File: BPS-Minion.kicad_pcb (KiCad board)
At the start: 2 copper layers, 219 parts, among them J10 TopConn, J11 TopConn, J2 BMS1OTP, J3 BMS2OTP, J4 Conn_01x24_Female, J5 Conn_01x24_Female, J6 TopConn, J7 TopConn, J8 TopConn, J9 TopConn, U10 LM321, U11 ADS7953SBDBT, U12 MIC5317-2.5xM5, U2 BQ7695201PFBR, U3 ISO1640BDR, U4 EL3H7, U5 BQ7695201PFBR, U6 ISO1640BDR, U7 EL3H7, U8 LM321, U9 ADS7953SBDBT

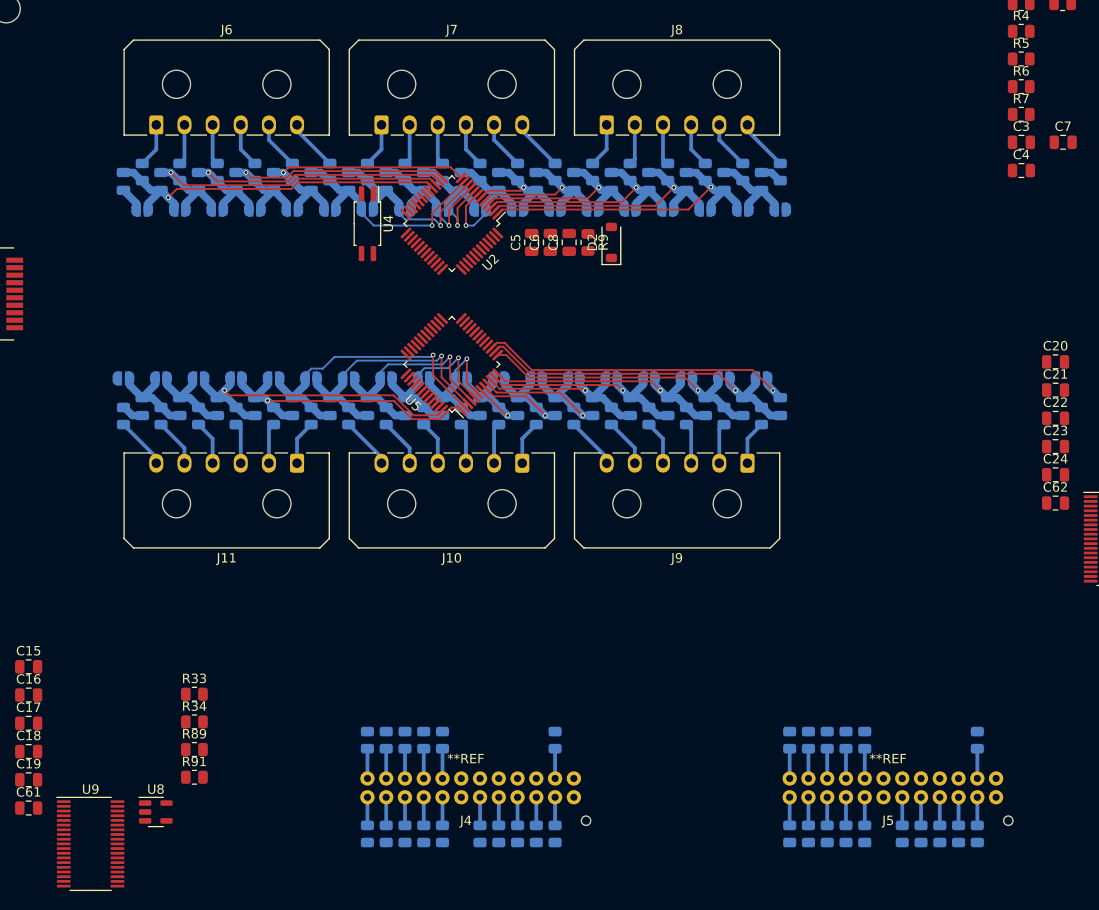
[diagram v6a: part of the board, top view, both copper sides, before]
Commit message: fix gnd2
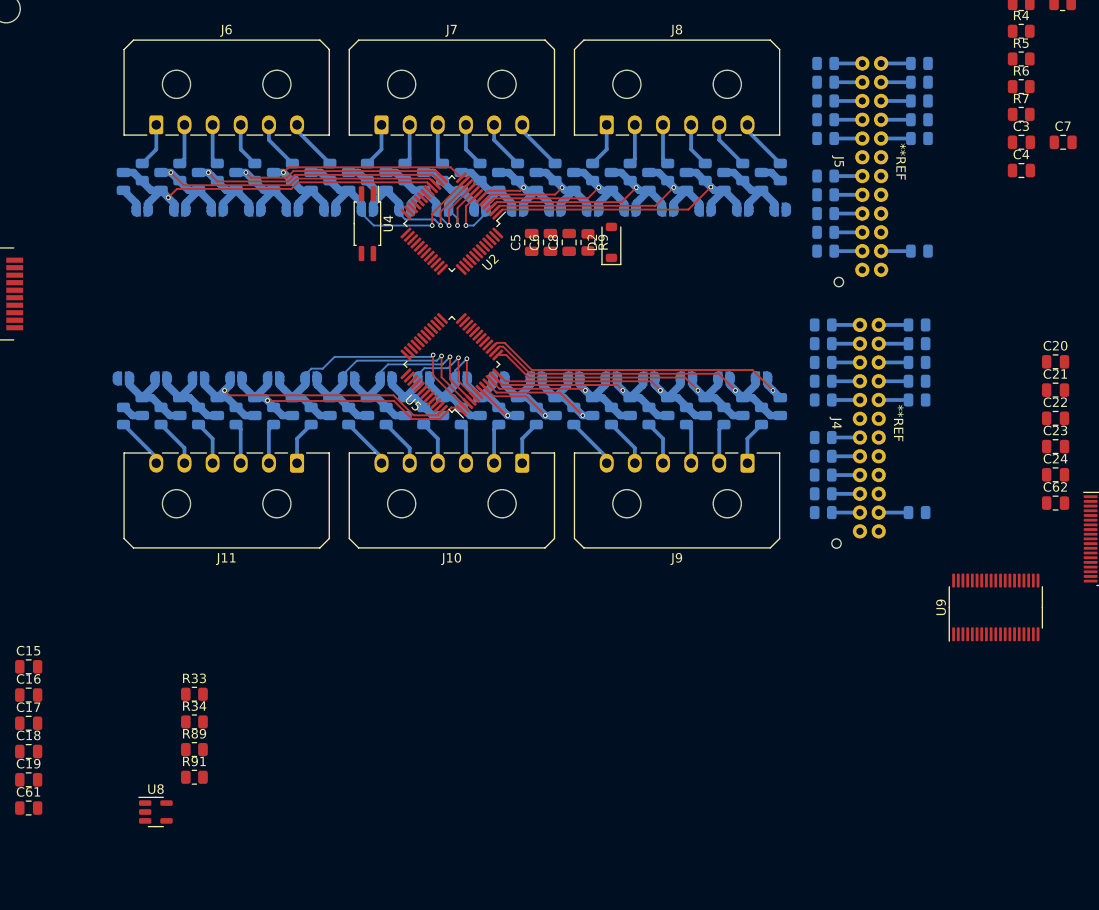
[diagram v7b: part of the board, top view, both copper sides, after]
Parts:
- moved U9 99.7 mm to (252.0, 152.4), turned to 90 degrees
- moved R43 82.2 mm to (233.8, 94.4), turned to 180 degrees
- moved R41 80.1 mm to (233.8, 96.4), turned to 180 degrees
- moved R39 78.1 mm to (233.8, 98.4), turned to 180 degrees
- moved R36 76.1 mm to (233.8, 100.4), turned to 180 degrees
- moved R38 74.2 mm to (233.8, 102.4), turned to 180 degrees
- moved R45 73.4 mm to (243.8, 94.4), turned to 0 degrees
- moved R27 73.4 mm to (243.6, 122.3), turned to 0 degrees
- moved R25 72.8 mm to (233.6, 122.3), turned to 180 degrees
- moved R47 71.1 mm to (243.8, 96.4), turned to 0 degrees
- moved R29 70.6 mm to (243.6, 124.3), turned to 0 degrees
- moved R40 70.6 mm to (233.8, 106.4), turned to 180 degrees
- moved R23 70.0 mm to (233.6, 124.3), turned to 180 degrees
- moved R42 68.9 mm to (233.8, 108.4), turned to 180 degrees
- moved R49 68.8 mm to (243.8, 98.4), turned to 0 degrees
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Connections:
- C40 pad 1: /BMS/cell15 -> GND2
- C41 pad 1: GND2 -> /BMS/cell16
- C41 pad 2: /BMS/cell15 -> GND2
- C42 pad 2: GND2 -> /BMS/cell16
- R68 pad 2: /BMS/cell15 -> GND2
- R69 pad 2: GND2 -> /BMS/cell16
- TP16 pad 2: /BMS/cell15 -> GND2
- TP17 pad 1: /BMS/cell15 -> GND2
- TP17 pad 2: GND2 -> /BMS/cell16
- TP18 pad 1: GND2 -> /BMS/cell16
- U2 pad 1: /BMS/cell15 -> GND2
- U2 pad 48: GND2 -> /BMS/cell16
- U5 pad 16: GND2 -> /BMS/cell16
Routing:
- net /BMS/cell15: track 33.9 -> 0.00 mm, vias 1 -> 0
- net GND2: track 10.0 -> 33.9 mm, vias 0 -> 1
- net /BMS/cell16: track 0.00 -> 10.0 mm

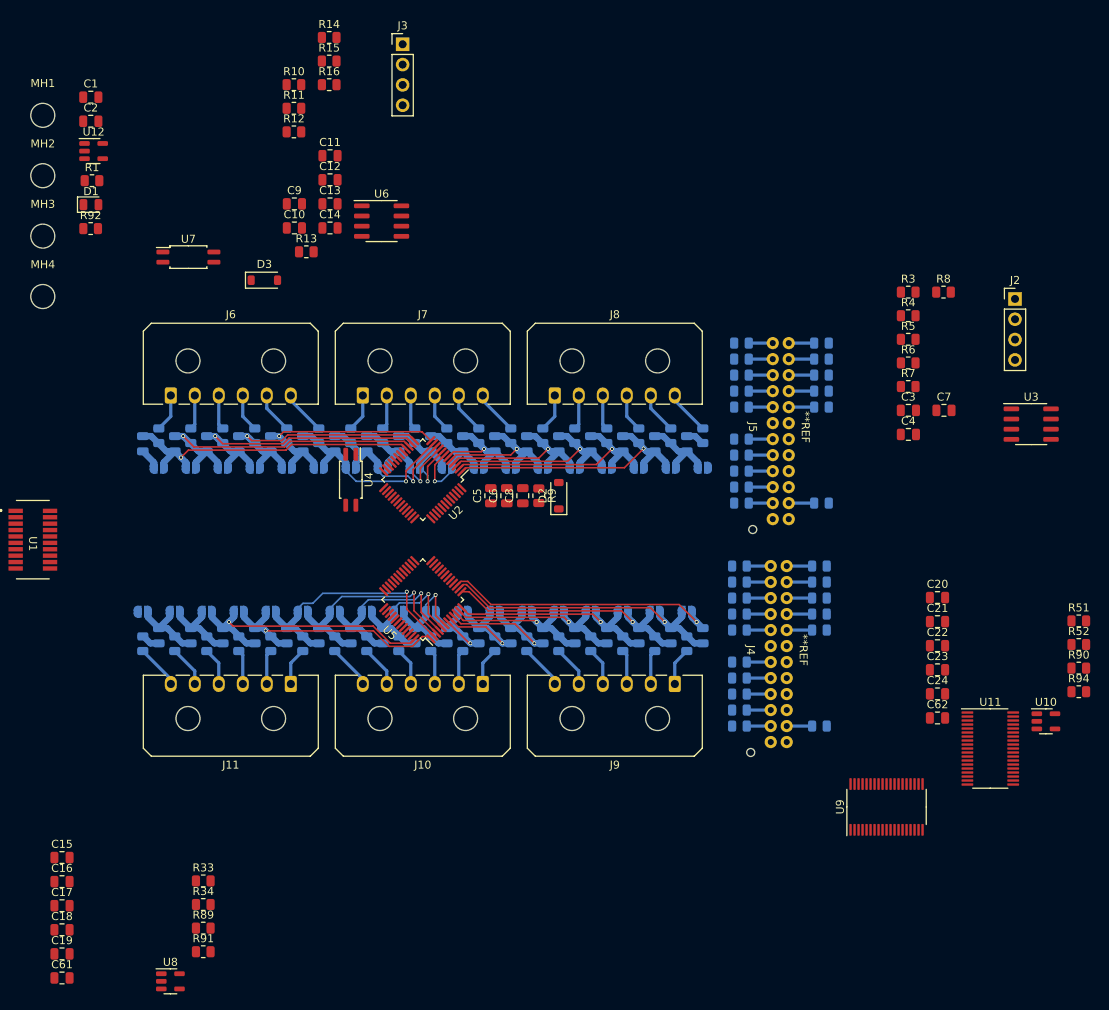
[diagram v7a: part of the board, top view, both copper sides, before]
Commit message: moved and grouped components, need to change temp connector adc and passives
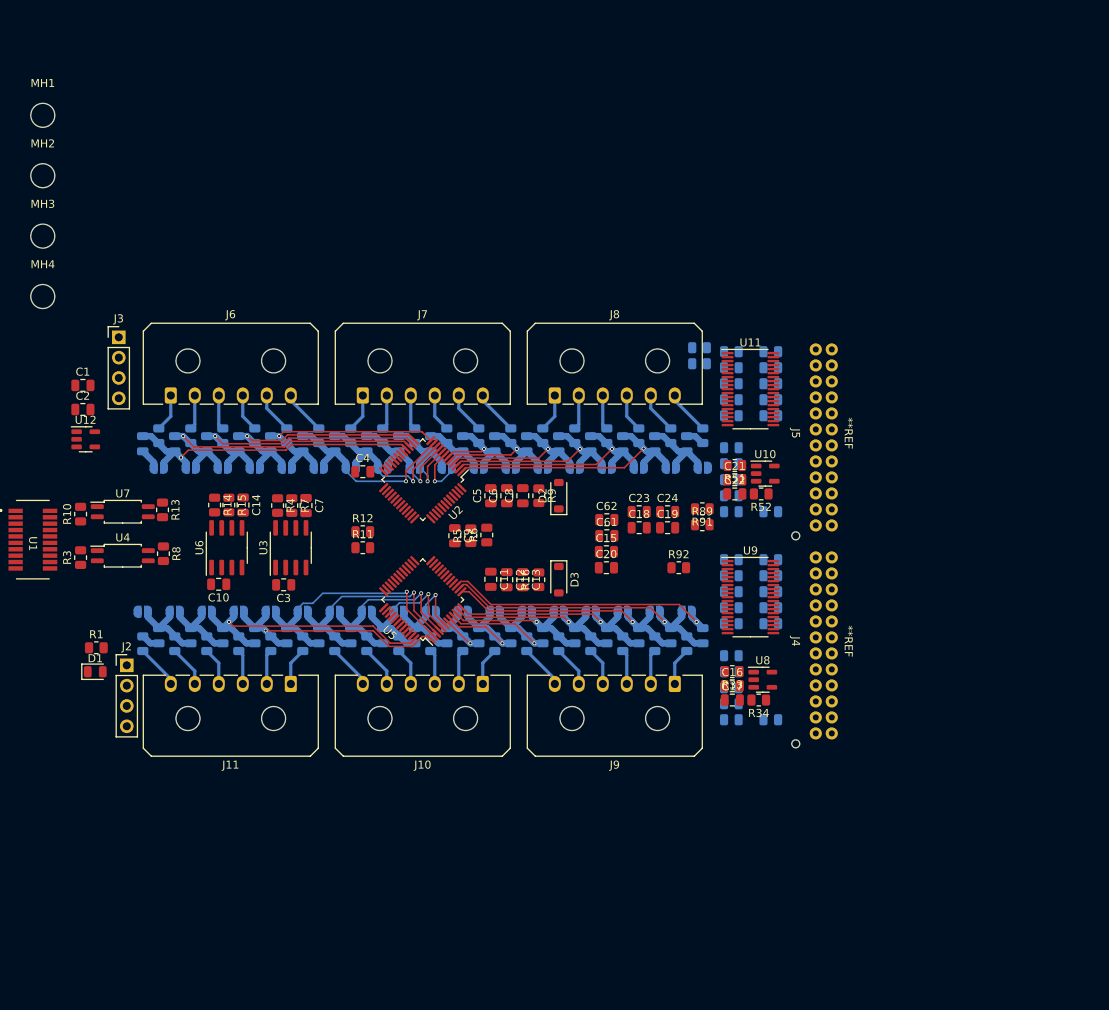
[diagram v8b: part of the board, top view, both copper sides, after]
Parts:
- R90, R94: moved to B.Cu
- moved J2 120.1 mm to (157.0, 134.7)
- moved R3 108.6 mm to (151.2, 121.2), turned to 90 degrees
- moved R8 102.8 mm to (161.6, 120.7), turned to -90 degrees
- moved U3 93.8 mm to (177.5, 120.0), turned to 90 degrees
- moved C19 92.6 mm to (224.6, 117.5)
- moved C18 87.9 mm to (221.1, 117.5)
- moved C61 87.7 mm to (217.0, 118.5)
- moved C17 87.6 mm to (232.7, 139.0)
- moved C16 87.3 mm to (232.7, 137.3)
- moved R92 84.9 mm to (226.0, 122.5)
- moved R91 83.4 mm to (228.9, 115.1), turned to 180 degrees
- moved U8 83.1 mm to (236.5, 136.5)
- moved R4 82.3 mm to (175.8, 114.7), turned to -90 degrees
- moved C3 81.1 mm to (176.6, 124.6), turned to 180 degrees
- moved C7 80.6 mm to (179.4, 114.7), turned to -90 degrees
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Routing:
- net /Temperature1/temp16: track 3.18 -> 0.00 mm
- net /Temperature/temp16: track 3.17 -> 0.00 mm
- net /Temperature1/temp8: track 3.09 -> 0.00 mm
- net /Temperature1/temp6: track 3.09 -> 0.00 mm
- net /Temperature/temp8: track 3.09 -> 0.00 mm
- net /Temperature/temp6: track 3.09 -> 0.00 mm
- net /Temperature/temp1: track 3.09 -> 0.00 mm
- net /Temperature1/temp7: track 3.09 -> 0.00 mm
- net /Temperature1/temp2: track 3.09 -> 0.00 mm
- net /Temperature1/temp1: track 3.09 -> 0.00 mm
- net /Temperature/temp7: track 3.09 -> 0.00 mm
- net /Temperature/temp2: track 3.09 -> 0.00 mm
- net /Temperature1/temp5: track 3.00 -> 0.00 mm
- net /Temperature1/temp12: track 3.00 -> 0.00 mm
- net /Temperature1/temp3: track 3.00 -> 0.00 mm
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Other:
- copper layers 2 -> 4
- board text added: "Using 0.5mm grid size"
